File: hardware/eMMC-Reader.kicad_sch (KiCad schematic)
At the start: 20 parts, among them J1 Conn_01x09_Socket, J2 USB3_A, U2 TXS02612, U3 W25X20CLSN

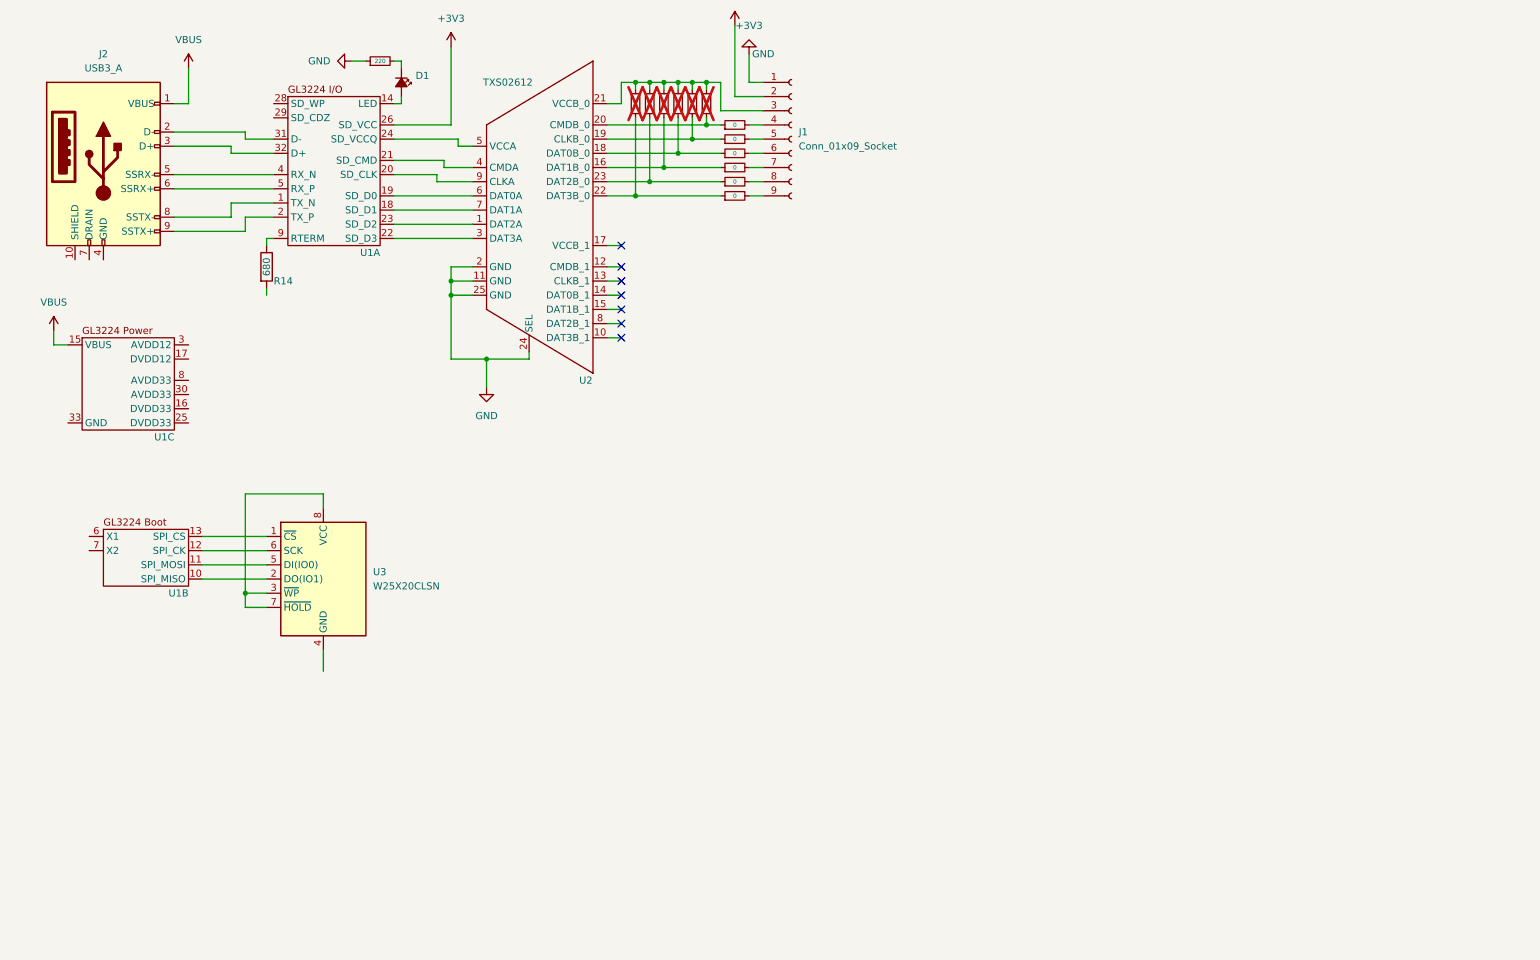
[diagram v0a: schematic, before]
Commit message: Finish up schematic (added switches and regulators); just some power caps to go
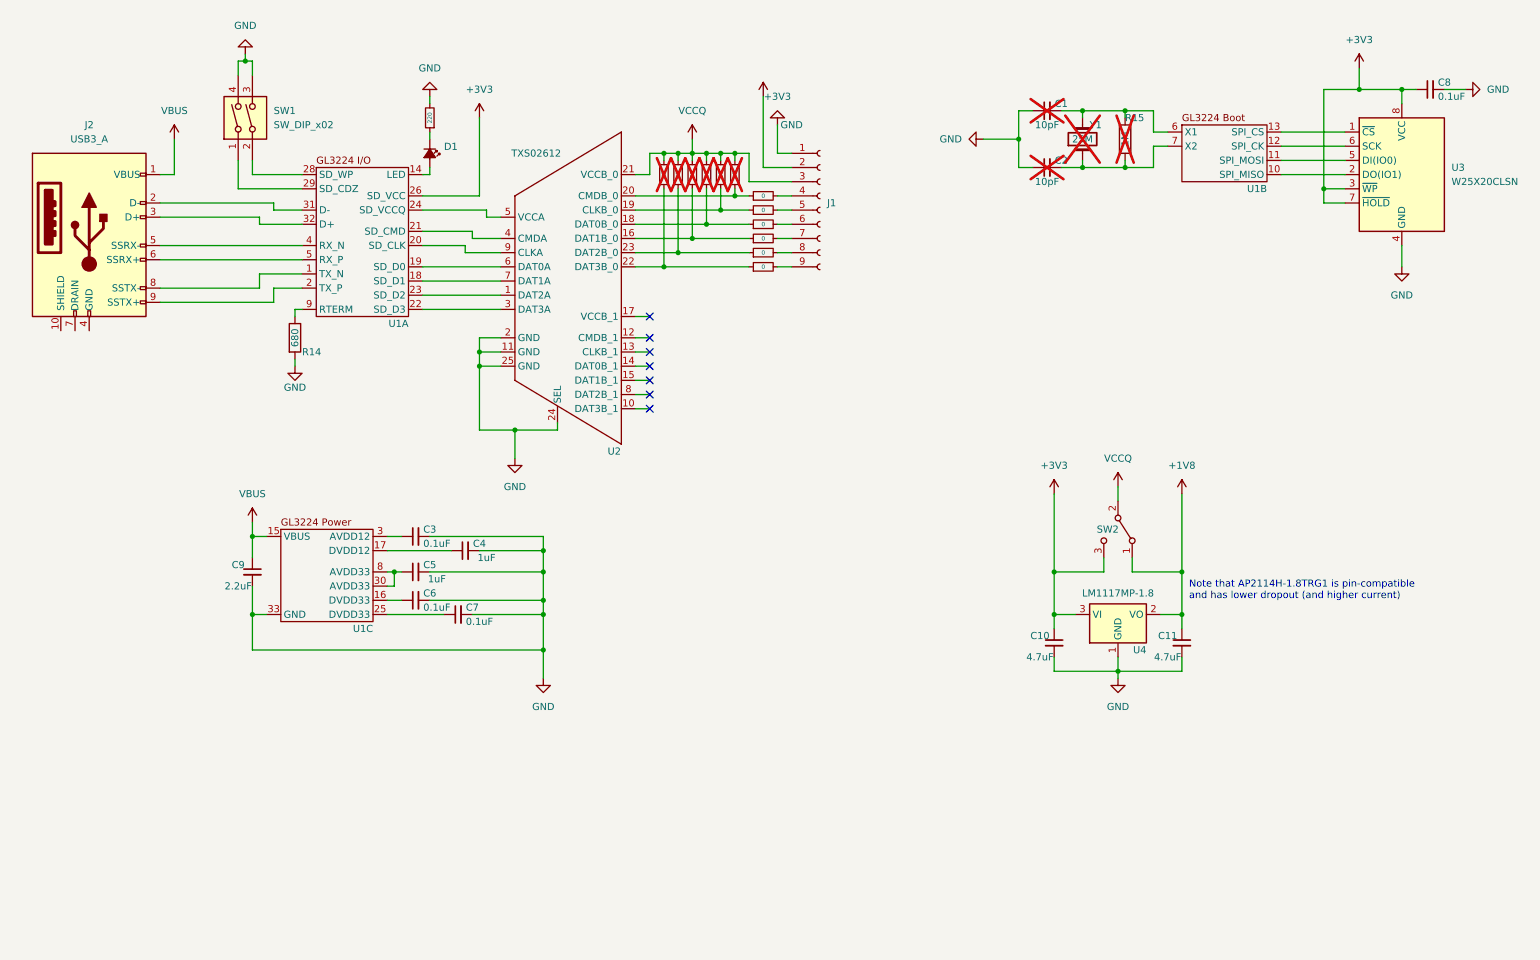
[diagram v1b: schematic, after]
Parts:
- added C1, C2: 10pF, symbol Device:C_Small
- added C10, C11: 4.7uF, symbol Device:C_Small
- added C3, C6, C7, C8: 0.1uF, symbol Device:C_Small
- added C4, C5: 1uF, symbol Device:C_Small
- added C9: 2.2uF, symbol Device:C_Small
- added R15: 1M, symbol Device:R
- added SW1: SW_DIP_x02, symbol Switch:SW_DIP_x02
- added SW2: SW_SPDT, symbol Switch:SW_SPDT
- added U4: LM1117MP-1.8, Package_TO_SOT_SMD:SOT-223-3_TabPin2, symbol Regulator_Linear:LM1117MP-1.8
- added Y1: 25M, symbol Device:Crystal
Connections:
- net +3V3: now also U3.3 (~{WP}), U3.7 (~{HOLD}), U3.8 (VCC), C10.1, C8.1, SW2.3 (C), U4.3 (VI)
- net GND: now also R13.2, R14.2, U1.33 (GND), U3.4 (GND), C1.1, C10.2, C11.2, C2.1, C3.2, C4.2, C5.2, C6.2, C7.2, C8.2, C9.2, SW1.3, SW1.4, U4.1 (GND); no longer R13.1
- net VBUS: now also C9.1
- net VCCQ: now reaches J1.3 (Pin_3), R10.2, R11.2, R12.2, R7.2, R8.2, R9.2, U2.21 (VCCB_0)
- net VCCQ: now also SW2.2 (B)
- net at D1.1 (K): now also R13.1; no longer R13.2
- net at U1.6 (X1): now also C1.2, R15.1, Y1.2
- net at U1.7 (X2): now also C2.2, R15.2, Y1.1
- net at U1.28 (SD_WP): now also SW1.2
- net at U1.29 (SD_CDZ): now also SW1.1
- net at U1.16 (DVDD33): now also C6.1
- net at U1.17 (DVDD12): now also C4.1
- net at U1.25 (DVDD33): now also C7.1
- net at U1.3 (AVDD12): now also C3.1
- net at U1.30 (AVDD33): now also U1.8 (AVDD33), C5.1
- new net +1V8: C11.1, SW2.1 (A), U4.2 (VO)
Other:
- note added: "Note that AP2114H-1.8TRG1 is pin-compatible and has lower dropout (and higher current)"
- moved on the sheet: D1, J1, J2, R14, U1A, U1B, U1C, U2, U3

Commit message: Finish schematic; partial layout for fully-featured board
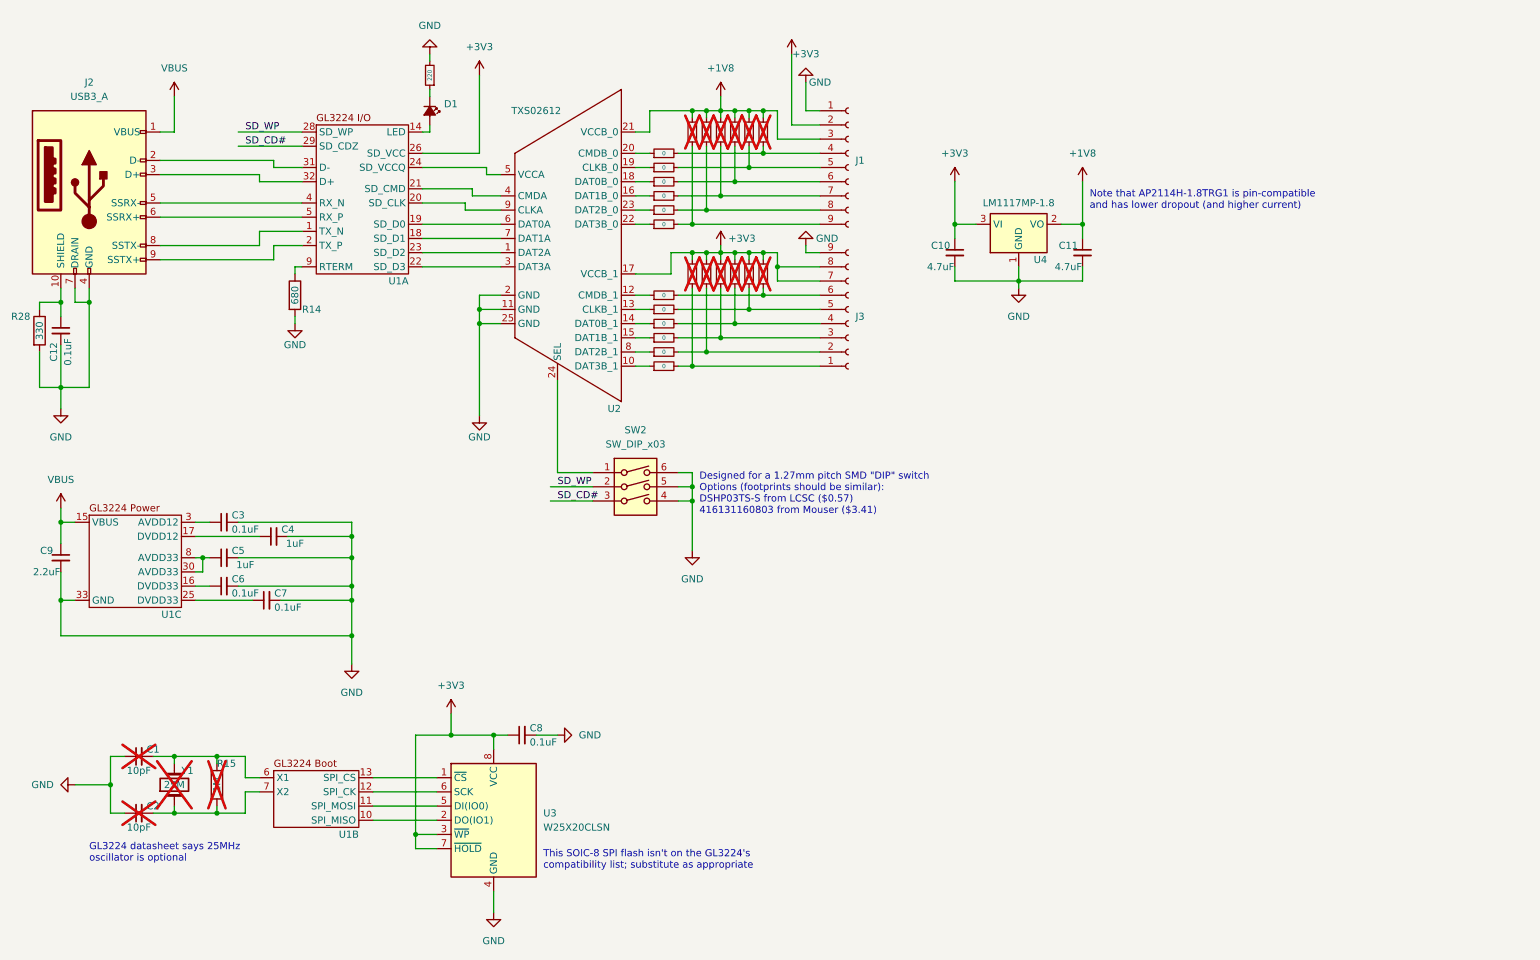
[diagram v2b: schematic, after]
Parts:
- removed SW1: SW_DIP_x02, symbol Switch:SW_DIP_x02
- removed SW2: SW_SPDT, symbol Switch:SW_SPDT
- added C12: 0.1uF, Capacitor_SMD:C_0603_1608Metric_Pad1.08x0.95mm_HandSolder, symbol Device:C_Small
- added J3: Conn_01x09_Socket, Connector_PinSocket_2.54mm:PinSocket_1x09_P2.54mm_Horizontal, symbol Connector:Conn_01x09_Socket
- added R16, R17, R18, R19, R20, R21: 0, Resistor_SMD:R_0603_1608Metric_Pad0.98x0.95mm_HandSolder, symbol Device:R_Small
- added R22, R23, R24, R25, R26, R27: 47, Resistor_SMD:R_0603_1608Metric_Pad0.98x0.95mm_HandSolder, symbol Device:R_Small
- added R28: 330, Resistor_SMD:R_0603_1608Metric_Pad0.98x0.95mm_HandSolder, symbol Device:R
- added SW2: SW_DIP_x03, symbol Switch:SW_DIP_x03
- C1, C10, C11, C2, C3, C4, C5, C6, C7, C8, C9: footprint (none) -> Capacitor_SMD:C_0603_1608Metric_Pad1.08x0.95mm_HandSolder
- D1: footprint (none) -> LED_SMD:LED_0603_1608Metric
- J1: footprint (none) -> Connector_PinSocket_2.54mm:PinSocket_1x09_P2.54mm_Horizontal
- J2: footprint (none) -> Connector_USB:USB3_A_Plug_Wuerth_692112030100_Horizontal
- R1, R10, R11, R12, R13, R14, R15, R2, R3, R4, R5, R6, R7, R8, R9: footprint (none) -> Resistor_SMD:R_0603_1608Metric_Pad0.98x0.95mm_HandSolder
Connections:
- net VCCQ is gone; now on net +1V8: J1.3 (Pin_3), R10.2, R11.2, R12.2, R7.2, R8.2, R9.2, U2.21 (VCCB_0)
- net +3V3: now also U2.17 (VCCB_1), J3.7 (Pin_7), J3.8 (Pin_8), R22.2, R23.2, R24.2, R25.2, R26.2, R27.2
- net GND: now also J2.4 (GND), J2.7 (DRAIN), C12.2, J3.9 (Pin_9), R28.2, SW2.4, SW2.5, SW2.6; no longer U2.24 (SEL)
- net at R4.1, U2.16 (DAT1B_0): no longer R9.1
- net at J1.7 (Pin_7), R4.2: now also R9.1
- net at R3.1, U2.18 (DAT0B_0): no longer R10.1
- net at R1.1, U2.20 (CMDB_0): no longer R12.1
- net at J1.4 (Pin_4), R1.2: now also R12.1
- net SD_CD#: now reaches U1.29 (SD_CDZ)
- net SD_CD#: now also SW2.3
- net SD_WP: now reaches U1.28 (SD_WP)
- net SD_WP: now also SW2.2
- net at R6.1, U2.22 (DAT3B_0): no longer R7.1
- net at R5.1, U2.23 (DAT2B_0): no longer R8.1
- net at R2.1, U2.19 (CLKB_0): no longer R11.1
- net at J1.5 (Pin_5), R2.2: now also R11.1
- net at J1.6 (Pin_6), R3.2: now also R10.1
- net at J1.8 (Pin_8), R5.2: now also R8.1
- net at J1.9 (Pin_9), R6.2: now also R7.1
- net at U2.10 (DAT3B_1): now also R21.1
- net at U2.12 (CMDB_1): now also R16.1
- net at U2.13 (CLKB_1): now also R17.1
- net at U2.14 (DAT0B_1): now also R18.1
- net at U2.15 (DAT1B_1): now also R19.1
- net at U2.8 (DAT2B_1): now also R20.1
- net at J2.10 (SHIELD): now also C12.1, R28.1
- new net: J3.1 (Pin_1), R21.2, R22.1
- new net: J3.2 (Pin_2), R20.2, R23.1
- new net: J3.5 (Pin_5), R17.2, R26.1
- new net: J3.4 (Pin_4), R18.2, R25.1
- new net: J3.3 (Pin_3), R19.2, R24.1
- new net: J3.6 (Pin_6), R16.2, R27.1
- new net: SW2.1, U2.24 (SEL)
- no-connect marks 7 -> 0
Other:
- note added: "Designed for a 1.27mm pitch SMD "DIP" switch Options (footprints should be similar): DSHP03TS-S from LCSC ($0.57) 416131160803 from Mouser ($3.41)"
- note added: "GL3224 datasheet says 25MHz oscillator is optional"
- note added: "This SOIC-8 SPI flash isn't on the GL3224's compatibility list; substitute as appropriate"
- moved on the sheet: C1, C10, C11, C2, C3, C4, C5, C6, C7, C8, C9, D1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
